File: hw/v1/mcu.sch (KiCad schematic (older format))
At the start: 35 parts, among them J5 SWD connector, J6 Conn_01x03, J7 Conn_01x03, U10 LP2985-3.3, U11 LP2985-5.0, U12 STM32F303RBTx, U13 DAC084S085, Y1 8MHz crystal

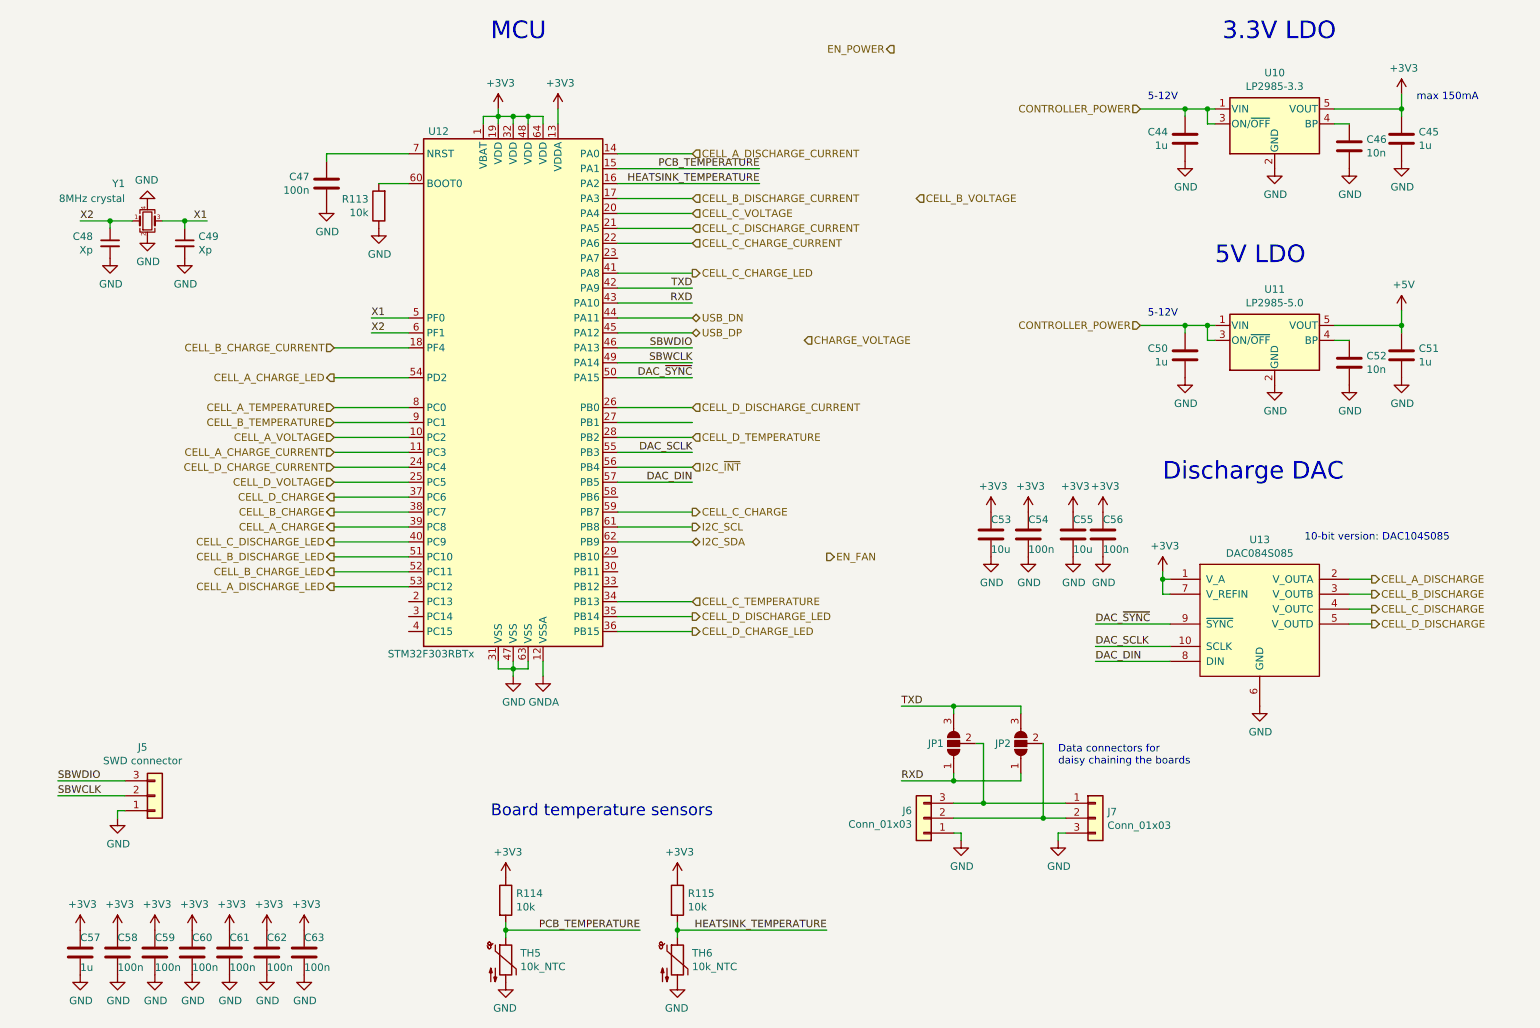
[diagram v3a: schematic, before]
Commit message: Layout done and MCU pins rearranged
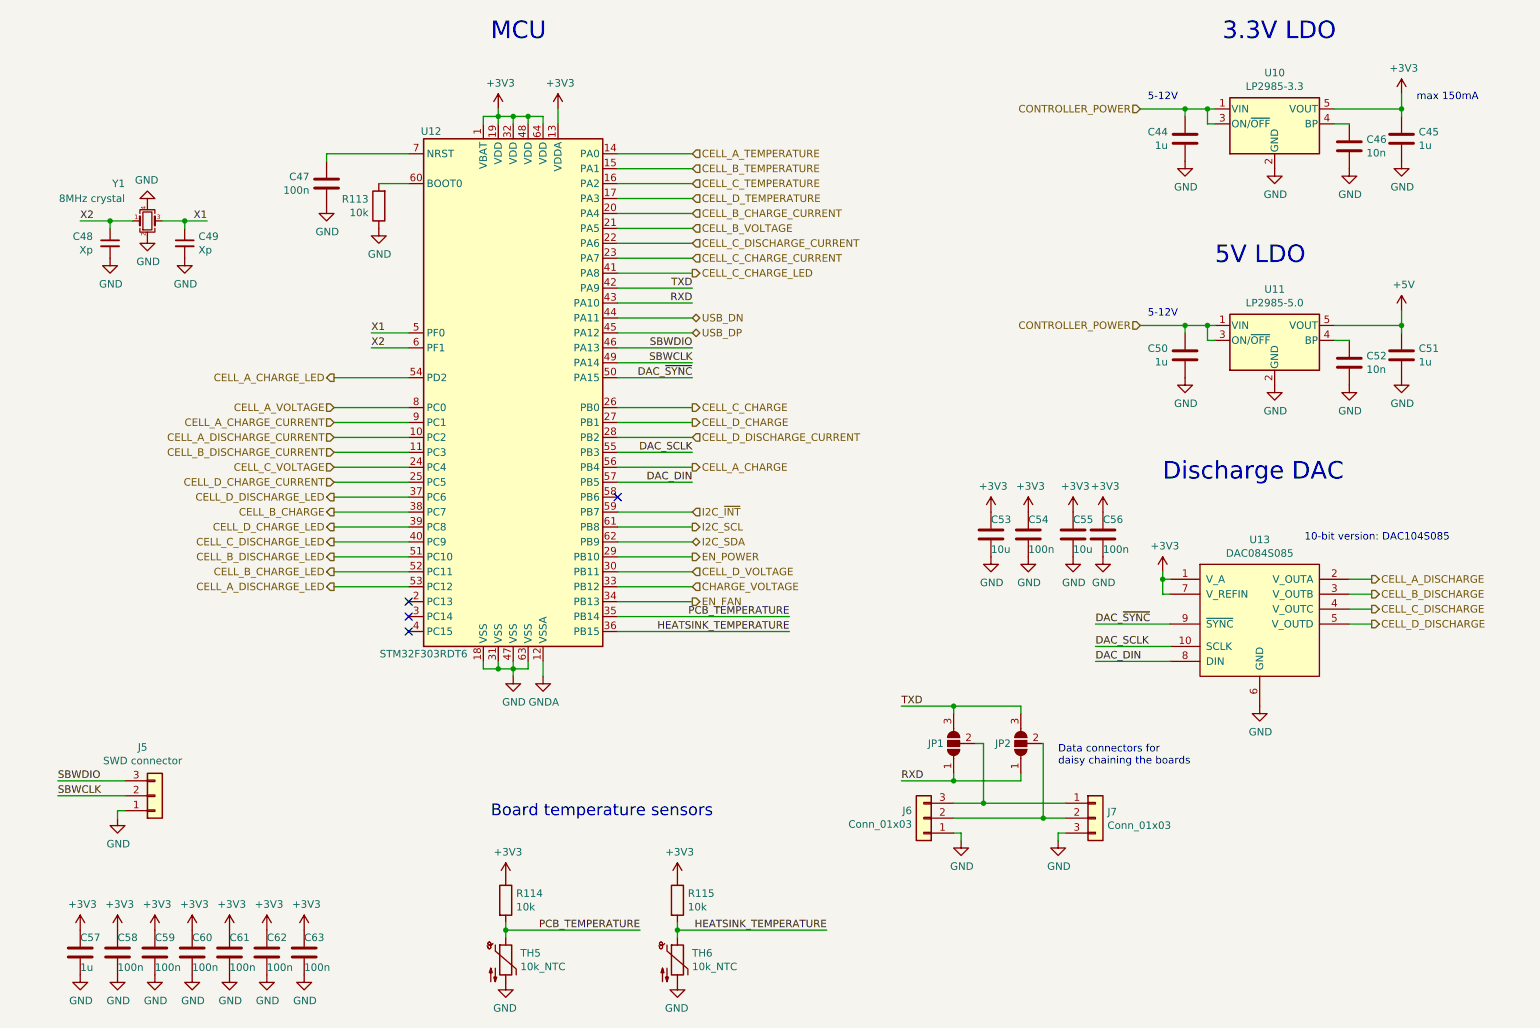
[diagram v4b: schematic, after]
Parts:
- removed U12: STM32F303RBTx, Package_QFP:LQFP-64_10x10mm_P0.5mm, symbol MCU_ST_STM32F3:STM32F303RBTx
- added U12: STM32F303RDT6, Package_QFP:LQFP-64_10x10mm_P0.5mm, symbol MCU_ST_STM32F3:STM32F303RDTx
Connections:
- net +3V3: now also U12.1 (VBAT), U12.13 (VDDA), U12.19 (VDD), U12.32 (VDD), U12.48 (VDD), U12.64 (VDD)
- net CELL_A_CHARGE: now also U12.56 (PB4)
- net CELL_A_CHARGE_CURRENT: now also U12.9 (PC1)
- net CELL_A_CHARGE_LED: now also U12.54 (PD2)
- net CELL_A_DISCHARGE_CURRENT: now also U12.10 (PC2)
- net CELL_A_DISCHARGE_LED: now also U12.53 (PC12)
- net CELL_A_TEMPERATURE: now also U12.14 (PA0)
- net CELL_A_VOLTAGE: now also U12.8 (PC0)
- net CELL_B_CHARGE: now also U12.38 (PC7)
- net CELL_B_CHARGE_CURRENT: now also U12.20 (PA4)
- net CELL_B_CHARGE_LED: now also U12.52 (PC11)
- net CELL_B_DISCHARGE_CURRENT: now also U12.11 (PC3)
- net CELL_B_DISCHARGE_LED: now also U12.51 (PC10)
- net CELL_B_TEMPERATURE: now also U12.15 (PA1)
- net CELL_B_VOLTAGE: now also U12.21 (PA5)
- net CELL_C_CHARGE: now also U12.26 (PB0)
- net CELL_C_CHARGE_CURRENT: now also U12.23 (PA7)
- net CELL_C_CHARGE_LED: now also U12.41 (PA8)
- net CELL_C_DISCHARGE_CURRENT: now also U12.22 (PA6)
- net CELL_C_DISCHARGE_LED: now also U12.40 (PC9)
- net CELL_C_TEMPERATURE: now also U12.16 (PA2)
- net CELL_C_VOLTAGE: now also U12.24 (PC4)
- net CELL_D_CHARGE: now also U12.27 (PB1)
- net CELL_D_CHARGE_CURRENT: now also U12.25 (PC5)
- net CELL_D_CHARGE_LED: now also U12.39 (PC8)
- net CELL_D_DISCHARGE_CURRENT: now also U12.28 (PB2)
- net CELL_D_DISCHARGE_LED: now also U12.37 (PC6)
- net CELL_D_TEMPERATURE: now also U12.17 (PA3)
- net CELL_D_VOLTAGE: now also U12.30 (PB11)
- net CHARGE_VOLTAGE: now also U12.33 (PB12)
- net DAC_DIN: now also U12.57 (PB5)
- net DAC_SCLK: now also U12.55 (PB3)
- net DAC_~SYNC: now also U12.50 (PA15)
- net EN_FAN: now also U12.34 (PB13)
- net EN_POWER: now also U12.29 (PB10)
- net GND: now also U12.18 (VSS), U12.31 (VSS), U12.47 (VSS), U12.63 (VSS)
- net GNDA: now also U12.12 (VSSA)
- net HEATSINK_TEMPERATURE: now also U12.36 (PB15)
- net I2C_SCL: now also U12.61 (PB8)
- net I2C_SDA: now also U12.62 (PB9)
- net I2C_~INT: now also U12.59 (PB7)
- net PCB_TEMPERATURE: now also U12.35 (PB14)
- net RXD: now also U12.43 (PA10)
- net SBWCLK: now also U12.49 (PA14)
- net SBWDIO: now also U12.46 (PA13)
- net TXD: now also U12.42 (PA9)
- net USB_DN: now also U12.44 (PA11)
- net USB_DP: now also U12.45 (PA12)
- net X1: now also U12.5 (PF0)
- net X2: now also U12.6 (PF1)
- net at R113.2: now also U12.60 (BOOT0)
- net at C47.1: now also U12.7 (NRST)
- no-connect marks 0 -> 4
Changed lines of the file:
@@
 encoding utf-8
 Sheet 7 7
-Title ""
-Date ""
-Rev ""
-Comp ""
+Title "CellShaper: MCU"
+Date "2020-07-15"
+Rev "v1"
+Comp "petrinm"
 Comment1 ""
 Comment2 ""
@@
 Wire Wire Line
 	4350 1300 4350 1400
-Text HLabel 2850 4100 0    50   Output ~ 0
+Text HLabel 5250 3700 2    50   Output ~ 0
 CELL_A_CHARGE
 Text HLabel 2850 4000 0    50   Output ~ 0
 CELL_B_CHARGE
-Text HLabel 5250 4000 2    50   Output ~ 0
+Text HLabel 5250 3300 2    50   Output ~ 0
 CELL_C_CHARGE
-Text HLabel 2850 3900 0    50   Output ~ 0
+Text HLabel 5250 3400 2    50   Output ~ 0
 CELL_D_CHARGE
+Text HLabel 2850 3300 0    50   Input ~ 0
+CELL_A_VOLTAGE
+Text HLabel 5250 2100 2    50   Input ~ 0
+CELL_B_VOLTAGE
+Text HLabel 2850 3700 0    50   Input ~ 0
+CELL_C_VOLTAGE
+Text HLabel 5250 4400 2    50   Input ~ 0
+CELL_D_VOLTAGE
+Text HLabel 2850 3400 0    50   Input ~ 0
+CELL_A_CHARGE_CURRENT
+Text HLabel 5250 2000 2    50   Input ~ 0
+CELL_B_CHARGE_CURRENT
+Text HLabel 5250 2300 2    50   Input ~ 0
+CELL_C_CHARGE_CURRENT
+Text HLabel 2850 3800 0    50   Input ~ 0
+CELL_D_CHARGE_CURRENT
 Text HLabel 2850 3500 0    50   Input ~ 0
-CELL_A_VOLTAGE
-Text HLabel 6750 1900 2    50   Input ~ 0
-CELL_B_VOLTAGE
-Text HLabel 5250 2000 2    50   Input ~ 0
-CELL_C_VOLTAGE
-Text HLabel 2850 3800 0    50   Input ~ 0
-CELL_D_VOLTAGE
+CELL_A_DISCHARGE_CURRENT
 Text HLabel 2850 3600 0    50   Input ~ 0
-CELL_A_CHARGE_CURRENT
-Text HLabel 2850 2900 0    50   Input ~ 0
-CELL_B_CHARGE_CURRENT
+CELL_B_DISCHARGE_CURRENT
 Text HLabel 5250 2200 2    50   Input ~ 0
-CELL_C_CHARGE_CURRENT
-Text HLabel 2850 3700 0    50   Input ~ 0
-CELL_D_CHARGE_CURRENT
+CELL_C_DISCHARGE_CURRENT
+Text HLabel 5250 3500 2    50   Input ~ 0
+CELL_D_DISCHARGE_CURRENT
 Text HLabel 5250 1600 2    50   Input ~ 0
-CELL_A_DISCHARGE_CURRENT
-Text HLabel 5250 1900 2    50   Input ~ 0
-CELL_B_DISCHARGE_CURRENT
-Text HLabel 5250 2100 2    50   Input ~ 0
-CELL_C_DISCHARGE_CURRENT
-Text HLabel 5250 3300 2    50   Input ~ 0
-CELL_D_DISCHARGE_CURRENT
-Text HLabel 2850 3300 0    50   Input ~ 0
 CELL_A_TEMPERATURE
-Text HLabel 2850 3400 0    50   Input ~ 0
+Text HLabel 5250 1700 2    50   Input ~ 0
 CELL_B_TEMPERATURE
-Text HLabel 5250 4600 2    50   Input ~ 0
+Text HLabel 5250 1800 2    50   Input ~ 0
 CELL_C_TEMPERATURE
 Text HLabel 2850 3100 0    50   Output ~ 0
@@
 Text HLabel 2850 4200 0    50   Output ~ 0
 CELL_C_DISCHARGE_LED
-Text HLabel 5250 4700 2    50   Output ~ 0
+Text HLabel 2850 3900 0    50   Output ~ 0
 CELL_D_DISCHARGE_LED
 Text HLabel 5250 2800 2    50   BiDi ~ 0
@@
 Wire Wire Line
 	4250 1350 4150 1350
-$Comp
-L MCU_ST_STM32F3:STM32F303RBTx U12
-U 1 1 5F27E0C0
-P 4050 3200
-F 0 "U12" H 3550 4950 50  0000 C CNN
-F 1 "STM32F303RBTx" H 3500 1450 50  0000 C CNN
-F 2 "Package_QFP:LQFP-64_10x10mm_P0.5mm" H 3450 1500 50  0001 R CNN
-F 3 "http://www.st.com/st-web-ui/static/active/en/resource/technical/document/datasheet/DM00058181.pdf" H 4050 3200 50  0001 C CNN
-	1    4050 3200
-	1    0    0    -1
-$EndComp
 Wire Wire Line
 	3150 1800 3350 1800
@@
 	5250 2900 4750 2900
 Wire Wire Line
-	3100 2700 3350 2700
+	3100 2800 3350 2800
 $Comp
 L Device:Crystal_GND24_Small Y1
@@
 	1    0    0    -1
 $EndComp
-Text HLabel 5250 4800 2    50   Output ~ 0
+Text HLabel 2850 4100 0    50   Output ~ 0
 CELL_D_CHARGE_LED
 Text HLabel 2850 4500 0    50   Output ~ 0
@@
 	1    0    0    -1
 $EndComp
-Text HLabel 6000 2850 2    50   Input ~ 0
+Text HLabel 5250 4500 2    50   Input ~ 0
 CHARGE_VOLTAGE
 $Comp
@@
 Wire Wire Line
 	5150 6800 6150 6800
-Text Label 5700 1800 2    50   ~ 0
-HEATSINK_TEMPERATURE
-Text Label 5700 1700 2    50   ~ 0
+Text Label 5900 4700 2    50   ~ 0
 PCB_TEMPERATURE
 Text HLabel 5250 2400 2    50   Output ~ 0
 CELL_C_CHARGE_LED
-Text HLabel 5250 3700 2    50   Input ~ 0
+Text HLabel 5250 4000 2    50   Input ~ 0
 I2C_~INT
 Wire Wire Line
@@
 $EndComp
 Wire Wire Line
-	3350 2800 3100 2800
+	3350 2900 3100 2900
 Text Label 5250 2500 2    50   ~ 0
 TXD
@@
 Wire Wire Line
 	5250 1900 4750 1900
-Wire Wire Line
-	2850 2900 3350 2900
-Text HLabel 5250 3500 2    50   Input ~ 0
+Text HLabel 5250 1900 2    50   Input ~ 0
 CELL_D_TEMPERATURE
 Wire Wire Line
@@
 	5250 2000 4750 2000
 Wire Wire Line
-	5700 1800 4750 1800
+	5250 1800 4750 1800
 Wire Wire Line
 	5250 1600 4750 1600
 Wire Wire Line
-	5250 4600 4750 4600
-Wire Wire Line
-	5250 4700 4750 4700
-Wire Wire Line
-	5250 4800 4750 4800
+	5900 4700 4750 4700
+Wire Wire Line
+	5900 4800 4750 4800
 Text Notes 8800 850  0    118  ~ 0
 3.3V LDO
@@
 	3950 1350 3950 1300
 Wire Wire Line
-	4750 1700 5700 1700
+	4750 1700 5250 1700
 $Comp
 L Device:C_Small C?
@@
 	1    0    0    -1
 $EndComp
-Text Label 3100 2700 0    50   ~ 0
+Text Label 3100 2800 0    50   ~ 0
 X1
-Text Label 3100 2800 0    50   ~ 0
+Text Label 3100 2900 0    50   ~ 0
 X2
 Text Label 2000 2050 2    50   ~ 0
@@
 Wire Wire Line
 	2800 1600 3350 1600
-Text HLabel 6600 900  0    50   Output ~ 0
+Text HLabel 5250 4300 2    50   Output ~ 0
 EN_POWER
-Text HLabel 6150 4300 2    50   Output ~ 0
+Text HLabel 5250 4600 2    50   Output ~ 0
 EN_FAN
 $Comp
@@
 Wire Wire Line
 	7600 6050 7750 6050
+Wire Wire Line
+	3850 5000 3850 5050
+Wire Wire Line
+	3850 5050 3950 5050
+Connection ~ 3950 5050
+$Comp
+L MCU_ST_STM32F3:STM32F303RDTx U12
+U 1 1 5F1D5B55
+P 4050 3200
+F 0 "U12" H 3500 4950 50  0000 C CNN
+F 1 "STM32F303RDT6" H 3450 1450 50  0000 C CNN
+F 2 "Package_QFP:LQFP-64_10x10mm_P0.5mm" H 3450 1500 50  0001 R CNN
+F 3 "http://www.st.com/st-web-ui/static/active/en/resource/technical/document/datasheet/DM00118585.pdf" H 4050 3200 50  0001 C CNN
+	1    4050 3200
+	1    0    0    -1
+$EndComp
+Wire Wire Line
+	5250 2300 4750 2300
+Wire Wire Line
+	5250 4400 4750 4400
+Text Label 5900 4800 2    50   ~ 0
+HEATSINK_TEMPERATURE
+Wire Wire Line
+	5250 4500 4750 4500
+Wire Wire Line
+	5250 4300 4750 4300
+Wire Wire Line
+	5250 4600 4750 4600
+NoConn ~ 4750 3900
+NoConn ~ 3350 4700
+NoConn ~ 3350 4600
+NoConn ~ 3350 4800
 $EndSCHEMATC
